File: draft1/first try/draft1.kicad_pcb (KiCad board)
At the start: 2 copper layers, 5 parts, among them IC1 74AVC4TD245PW,118, IC2 74AVC4TD245PW,118, J1 Conn_01x24

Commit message: made pcb ratsnest
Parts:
- removed IC1, IC2: 74AVC4TD245PW,118, SamacSys_Parts:SOP65P640X110-16N
- added C1: 10uF, Capacitor_SMD:C_0402_1005Metric, F.Cu at (269.3, 110.5)
- added C10: LED, Capacitor_SMD:C_0402_1005Metric, F.Cu at (272.3, 110.0)
- added C11: LED, Capacitor_SMD:C_0402_1005Metric, F.Cu at (266.4, 111.9)
- added C12: 47pF, Capacitor_SMD:C_0402_1005Metric, F.Cu at (270.4, 108.0)
- added C13: NP, Capacitor_SMD:C_0402_1005Metric, F.Cu at (176.4, 170.5)
- added C14: NP, Capacitor_SMD:C_0402_1005Metric, F.Cu at (175.8, 175.2)
- added C15: NP, Capacitor_SMD:C_0402_1005Metric, F.Cu at (179.3, 170.5)
- added C16: NP, Capacitor_SMD:C_0402_1005Metric, F.Cu at (176.4, 172.5)
- added C17: NP, Capacitor_SMD:C_0402_1005Metric, F.Cu at (174.1, 177.7)
- added C18: NP, Capacitor_SMD:C_0402_1005Metric, F.Cu at (180.4, 168.0)
- added C19: NP, Capacitor_SMD:C_0402_1005Metric, F.Cu at (182.3, 170.0)
- added C2: NP, Capacitor_SMD:C_0402_1005Metric, F.Cu at (269.3, 112.5)
- added C20: NP, Capacitor_SMD:C_0402_1005Metric, F.Cu at (178.7, 174.5)
- added C21: NP, Capacitor_SMD:C_0402_1005Metric, F.Cu at (182.3, 171.9)
- added C22: NP, Capacitor_SMD:C_0402_1005Metric, F.Cu at (177.0, 177.2)
- added C23: 0.1uF, Capacitor_SMD:C_0402_1005Metric, F.Cu at (179.3, 172.5)
- added C24: NP, Capacitor_SMD:C_0402_1005Metric, F.Cu at (181.6, 174.5)
- added C25: 0.1uF, Capacitor_SMD:C_0402_1005Metric, F.Cu at (142.4, 177.1)
- added C26: 0.1uF, Capacitor_SMD:C_0402_1005Metric, F.Cu at (147.5, 171.5)
- added C27: 0.1uF, Capacitor_SMD:C_0402_1005Metric, F.Cu at (142.4, 173.1)
- added C28: CAP0805, Capacitor_SMD:C_0402_1005Metric, F.Cu at (142.4, 175.1)
- added C29: 4.7uF, Capacitor_SMD:C_0402_1005Metric, F.Cu at (145.3, 173.5)
- added C3: 10uF, Capacitor_SMD:C_0402_1005Metric, F.Cu at (272.8, 104.1)
- added C4: 0.1uF, Capacitor_SMD:C_0402_1005Metric, F.Cu at (260.6, 112.4)
- added C5: 0.1uF, Capacitor_SMD:C_0402_1005Metric, F.Cu at (264.6, 109.9)
- added C6: 4.7uF, Capacitor_SMD:C_0402_1005Metric, F.Cu at (268.8, 106.0)
- added C7: 10nF, Capacitor_SMD:C_0402_1005Metric, F.Cu at (272.8, 102.1)
- added C8: 0.1uF, Capacitor_SMD:C_0402_1005Metric, F.Cu at (263.5, 112.4)
- added C9: 47pF, Capacitor_SMD:C_0402_1005Metric, F.Cu at (267.5, 108.5)
- added JA1: fpga_header_1, Connector_PinHeader_2.54mm:PinHeader_2x06_P2.54mm_Vertical, F.Cu at (128.8, 169.3)
- added JB1: fpga_header_1, Connector_PinHeader_2.54mm:PinHeader_2x06_P2.54mm_Vertical, F.Cu at (136.0, 169.3)
- added L1: HZ0805E601R-10, Inductor_SMD:L_0805_2012Metric, F.Cu at (266.3, 100.0)
- added P3: Conn_01x02, Connector_PinHeader_2.54mm:PinHeader_1x02_P2.54mm_Vertical, F.Cu at (248.0, 108.4)
- added P4: Conn_01x24, Connector_PinHeader_2.54mm:PinHeader_1x24_P2.54mm_Vertical, F.Cu at (128.8, 100.9)
- added P5: Conn_01x02, Connector_PinHeader_2.54mm:PinHeader_1x02_P2.54mm_Vertical, F.Cu at (172.7, 169.3)
- added R1: NP, Resistor_SMD:R_0603_1608Metric, F.Cu at (270.5, 99.8)
- added R12: NP, Resistor_SMD:R_0603_1608Metric, F.Cu at (177.0, 168.2)
- added R13: NP, Resistor_SMD:R_0603_1608Metric, F.Cu at (172.3, 175.4)
- added R14: NP, Resistor_SMD:R_0603_1608Metric, F.Cu at (170.6, 177.9)
- added R2: NP, Resistor_SMD:R_0603_1608Metric, F.Cu at (266.1, 102.8)
- added R3: 27, Resistor_SMD:R_0603_1608Metric, F.Cu at (257.2, 110.2)
- added R4: 270, Resistor_SMD:R_0603_1608Metric, F.Cu at (257.2, 112.7)
- added R5: 270, Resistor_SMD:R_0603_1608Metric, F.Cu at (261.2, 110.2)
- added R6: 27, Resistor_SMD:R_0603_1608Metric, F.Cu at (252.3, 107.4)
- added R9: NP, Resistor_SMD:R_0603_1608Metric, F.Cu at (152.3, 168.2)
- added U1: LP5907MFX-1.5, Package_TO_SOT_SMD:SOT-23-5, F.Cu at (252.7, 111.2)
- added U10: LTC4123, Package_DFN_QFN:DFN-6-1EP_2x2mm_P0.5mm_EP0.6x1.37mm, F.Cu at (148.2, 168.7)
- added U2: 74AVC1T45GS,132, SamacSys_Parts:74LVC1G3157GS132, F.Cu at (265.7, 105.8)
- added U3: FT231XS-U, Package_SO:SSOP-20_3.9x8.7mm_P0.635mm, F.Cu at (260.1, 103.7)
- added U4: 74AVC1T45GS,132, SamacSys_Parts:74LVC1G3157GS132, F.Cu at (269.7, 103.3)
- added U5: 74AVC4TD245PW,118, SamacSys_Parts:SOP65P640X110-16N, F.Cu at (135.6, 102.0)
- added U6: 74AVC4TD245PW,118, SamacSys_Parts:SOP65P640X110-16N, F.Cu at (144.5, 102.0)
- added U7: ADT7302ARMZ, SamacSys_Parts:SOP65P490X110-8N, F.Cu at (165.2, 176.7)
- added U8: scum3, SCUM:QFP-100_2x3_Pitch0.15mm, F.Cu at (166.1, 170.7)
- added U9AB1: MPU-9250, Sensor_Motion:InvenSense_QFN-24_3x3mm_P0.4mm, F.Cu at (143.5, 169.5)
- J1: value Conn_01x24 -> 47346-0001; footprint Connector_PinHeader_2.54mm:PinHeader_1x24_P2.54mm_Vertical -> Connector_USB:USB_Micro-B_Molex_47346-0001
- moved J1 154.8 mm to (250.9, 101.7)
- moved R7 46.9 mm to (155.0, 99.8)
- moved R8 41.7 mm to (151.0, 99.8)
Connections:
- J1 pad 2: Net-(J1-Pad2) -> /U_uart/D_N
- J1 pad 3: Net-(J1-Pad3) -> /U_uart/D_P
- J1 pad 4: Net-(J1-Pad4) -> (no net)
- J1 pad 5: Net-(J1-Pad5) -> GND
- J1 pad 6: /LF_CLK_33 -> (no net)
- R7 pad 1: /HARD_RESET_33 -> /U_scan_chain_boot/HARD_RESET_33
- R7 pad 2: /HR -> /U_scan_chain_boot/HARD_RESET
- R8 pad 1: /HARD_RESET_33 -> /U_scan_chain_boot/HARD_RESET_33

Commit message: placed some footprints
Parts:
- C16, C17, C21, C25, C27, C28, C29, JA1, JB1, R14, R9, U7: moved to B.Cu
- moved R1 156.8 mm to (115.6, 124.5)
- moved R2 152.8 mm to (115.6, 129.5)
- moved U3 139.8 mm to (120.7, 113.3)
- moved U1 123.1 mm to (134.6, 146.1)
- moved C1 119.4 mm to (151.2, 92.7)
- moved C11 119.4 mm to (148.3, 94.1)
- moved C2 119.4 mm to (151.2, 94.7)
- moved C4 119.4 mm to (142.5, 94.6)
- moved C6 119.4 mm to (150.7, 88.2)
- moved C9 119.4 mm to (149.4, 90.7)
- moved R3 119.4 mm to (139.0, 92.4)
- moved R4 119.4 mm to (139.0, 94.9)
- moved R5 119.4 mm to (143.1, 92.4)
- moved C10 119.4 mm to (154.1, 92.2)
- moved C12 119.4 mm to (152.3, 90.2)
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
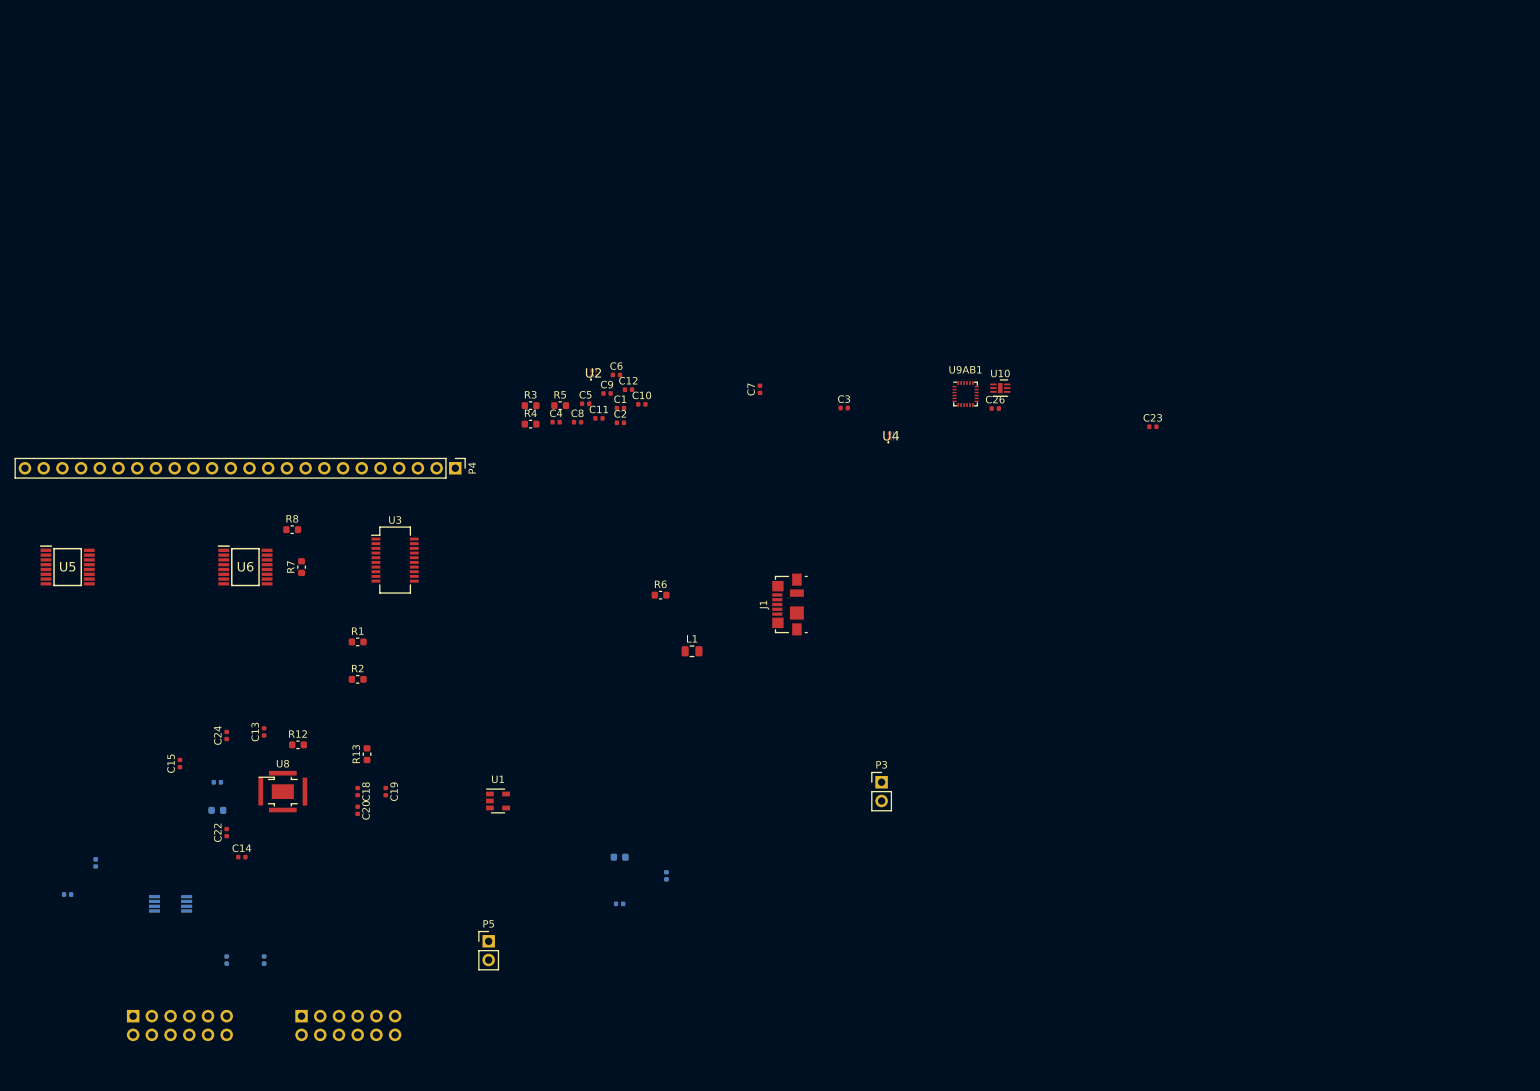
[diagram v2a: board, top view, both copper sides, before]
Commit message: placed footprints
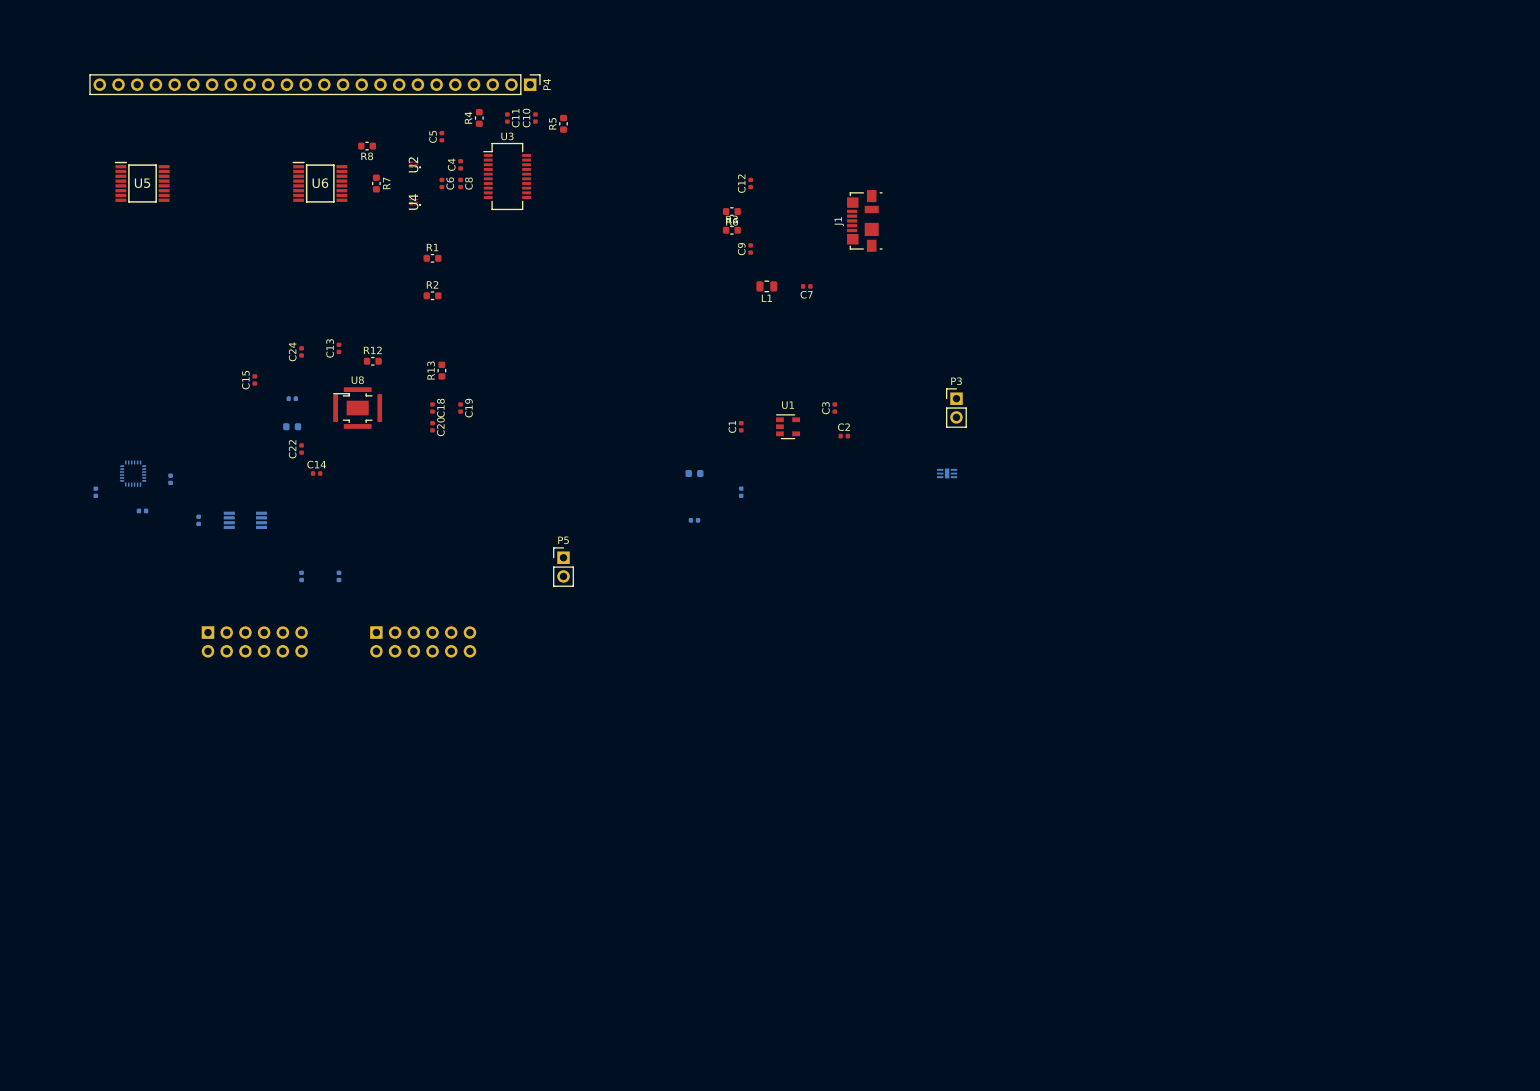
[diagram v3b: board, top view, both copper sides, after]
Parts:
- C23, C26, U10, U9AB1: moved to B.Cu
- moved C23 130.2 mm to (94.0, 108.0), turned to 270 degrees
- moved C26 122.6 mm to (80.0, 104.1), turned to 270 degrees
- moved U9AB1 113.5 mm to (85.1, 101.6)
- moved U4 72.1 mm to (123.2, 64.8), turned to 90 degrees
- moved U1 64.3 mm to (174.0, 95.2)
- moved U3 54.3 mm to (135.9, 61.3)
- moved C18 53.1 mm to (125.7, 92.7)
- moved P4 53.1 mm to (139.0, 48.8)
- moved C13 53.1 mm to (113.0, 84.6)
- moved C19 53.1 mm to (129.5, 92.7)
- moved C20 53.1 mm to (125.7, 95.2)
- moved C21 53.1 mm to (106.7, 91.4)
- moved C27 53.1 mm to (90.2, 102.4), turned to 270 degrees
- moved C28 53.1 mm to (161.3, 108.0), turned to 180 degrees
- moved C29 53.1 mm to (167.6, 104.1)
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
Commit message: edge cut
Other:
- board outline added: 142.2 x 96.5 mm
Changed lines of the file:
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@@
   (general
     (thickness 1.6)
-    (drawings 0)
+    (drawings 4)
     (tracks 0)
     (zones 0)
@@
     )
   )
+  (gr_line (start 214.63 39.37) (end 214.63 135.89) (layer Edge.Cuts) (width 0.1))
+  (gr_line (start 72.39 39.37) (end 214.63 39.37) (layer Edge.Cuts) (width 0.1))
+  (gr_line (start 72.39 135.89) (end 72.39 39.37) (layer Edge.Cuts) (width 0.1))
+  (gr_line (start 214.63 135.89) (end 72.39 135.89) (layer Edge.Cuts) (width 0.1))
 )

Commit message: tried autorouter
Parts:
- moved C26 9.16 mm to (85.1, 96.5), turned to 0 degrees
- moved R14 8.89 mm to (97.8, 95.2), turned to 270 degrees
- moved C25 8.13 mm to (80.0, 101.6), turned to 90 degrees
- moved R12 7.82 mm to (119.4, 78.7)
- moved C13 7.14 mm to (113.0, 77.5), turned to 180 degrees
- moved C10 6.84 mm to (146.1, 55.9)
- moved C11 6.84 mm to (142.2, 55.9)
- moved R5 6.84 mm to (149.9, 56.7)
- moved U3 6.84 mm to (142.2, 63.8)
- moved R4 6.84 mm to (138.4, 55.9)
- moved C24 6.35 mm to (104.1, 80.0)
- moved C19 5.08 mm to (134.6, 92.7), turned to 90 degrees
- moved C21 5.08 mm to (101.6, 91.4), turned to 90 degrees
- moved R13 5.08 mm to (132.1, 87.6), turned to 270 degrees
- moved C14 5.08 mm to (104.9, 101.6), turned to 180 degrees
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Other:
- net class smaller added: clearance 0.05, trace_width 0.2, via_dia 0.4, via_drill 0.3
